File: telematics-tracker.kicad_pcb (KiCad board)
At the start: 4 copper layers, 82 x 62 mm, 227 parts, among them J1 WAFER-MX3.0-12PZZ, J2 B3B-XH-A, Q1 AM2390N-TP, Q10 MMBT3904, Q11 MMBT3904, Q12 MMBT3904, Q13 MMBT3906, Q14 MMBT3904, Q2 AM2390N-TP, Q3 AO3401A, Q4 MMBT3904, Q5 MMBT3904, Q6 MMBT3904, Q7 MMBT3904, Q8 MMBT3904, Q9 MMBT3904, U1 EC200UCNAA-N05-SGNSA, U2 AT32F403ACGT7, U3 QMI8658B, U4 SIT1051AT/3, U5 EG11752, U6 BQ25606RGER, U7 GD25Q64ESIGR, U8 TXB0104PWR, U9 ME6211C33M5G, X1 NANO-SIM, X2 MFF2-eSIM-pads, Y1 8MHz, Y2 32.768kHz

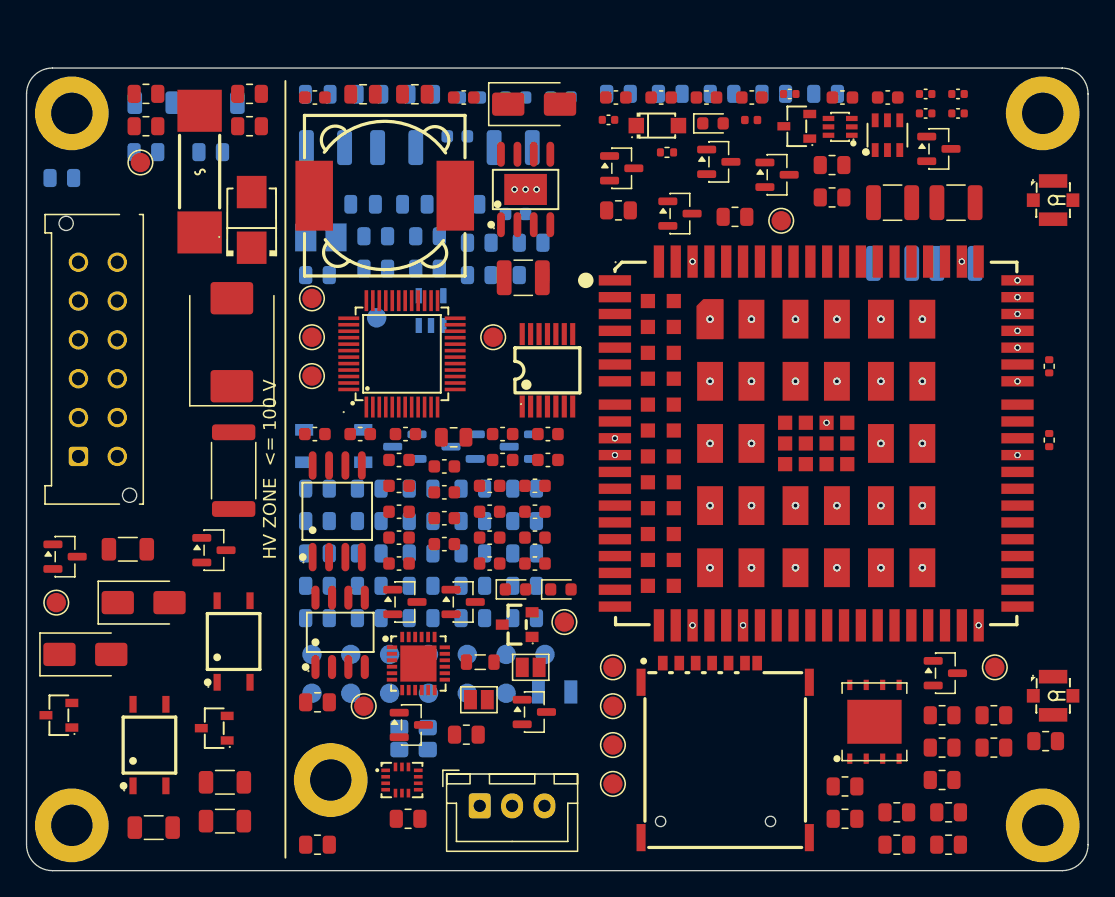
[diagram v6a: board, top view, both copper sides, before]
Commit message: F-21 RETRACTED (my misread); antennas selected; 8 of 8 floorplan checks pass
F-21 was wrong and the error was mine. I read the pdftotext -layout dump, where
0R and 100 pF share a row and NM NM sit below, and took the 100 pF for a shunt.
Rendering page 69 at 200 dpi shows it has VERTICAL plates in the signal line: it
is a SERIES DC BLOCK, and the 47 nH injects VDD on the ANTENNA side of it. The
module pin is DC-isolated by construction; there was never a conflict.
Corroborated by Antenna Design Guide V3.3 5.1 note 5, which also asks for
>= 56 nH - so L4 is 68 nH, not figure 31's 47 nH. Table 40 does not list
ANT_GNSS at all, so there is no published DC rating for pin 47, which is the
real reason the block is mandatory.

Schematic corrected: C84 100 pF is in SERIES and ALWAYS FITTED (depopulating it
opens the antenna; 1.0 ohm at 1575 MHz). Only L4/R90/C83 are DNP. Chain verified
in the netlist: U1.47 -> R72 -> C84 -> AF2.3, bias injected at ANT_GNSS_F.
C84 anchored inline in the RF corridor and check 1 extended to validate every
inline element. checkpins caught a real short while doing this - the first
bias-T placement merged GNSS_BIAS into USIM_VDD.

Parts: C1546 100pF C0G (always fitted), C3221844 Murata LQW15AN68NG80D 68 nH
WIREWOUND SRF 2.5 GHz (every multilayer 0402 at this value has SRF ~1.1 GHz and
is capacitive at 1575 MHz), C25077 10R, C60474 0.1uF.

Antennas: LTE C496569 Bat Wireless BW4GFNX39-15B1, 700-2700 MHz continuous,
120 mm IPEX-1 pigtail, 5536 stock. Runner-up C22467619 rejected - it omits B40,
which Jio uses heavily in India.

GNSS C784386 - but this is a DEVIATION NEEDING A DECISION: no passive 25x25
patch with a U.FL pigtail exists in LCSC stock, so the recommendation is ACTIVE
(LNA 21.5 dB, 1.8-3.6 V, 4.3 mA). That makes the bias-T MANDATORY rather than
DNP for the internal build. Passive alternative C784398 has solder pins and no
cable, needing a hand-added pigtail and a 60-70 mm lid ground plane.

Quectel's < 17 dB LNA limit is a recommendation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
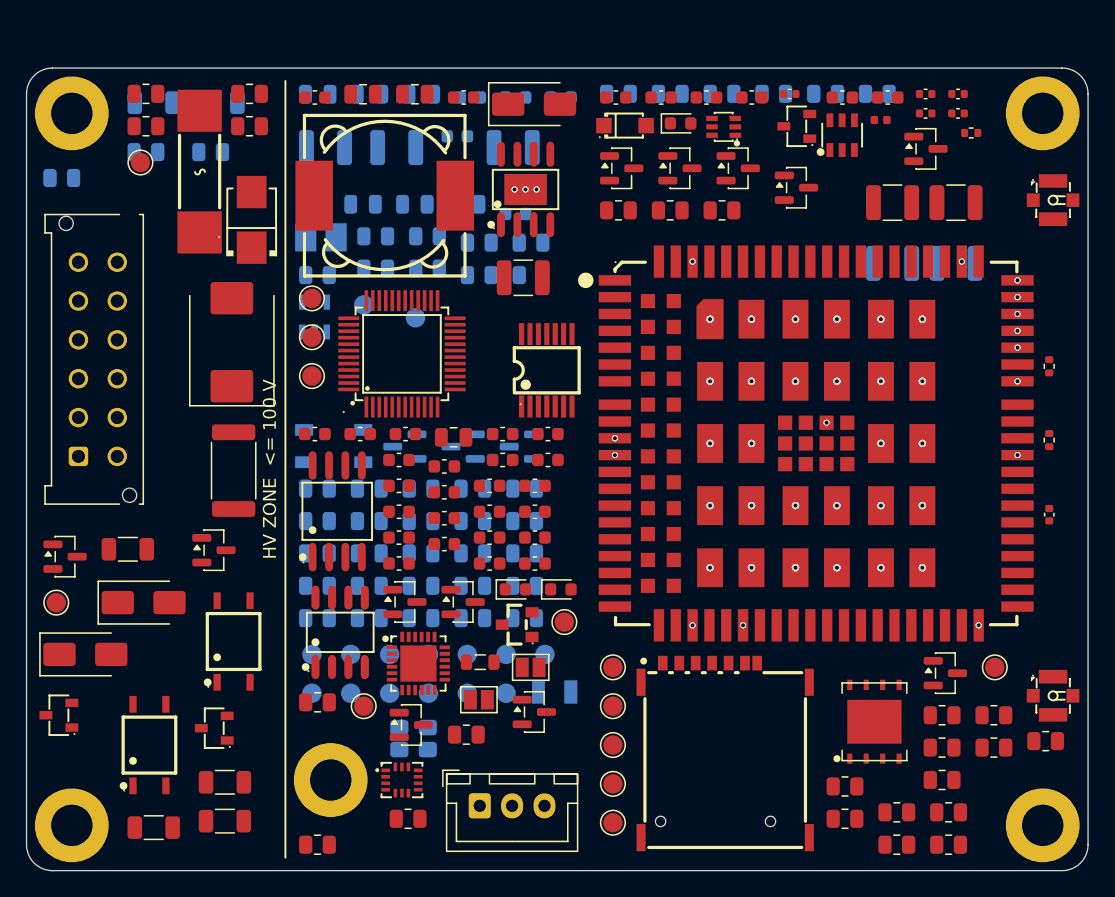
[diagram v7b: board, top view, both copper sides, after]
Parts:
- C83: value 100nF DNP -> 100nF
- C84: value 100pF DNP -> 100pF C0G
- L4: value 47nH DNP -> 68nH
- R65, TP22: moved to B.Cu
- R90: value 10R DNP -> 10R
- moved R65 63.4 mm to (45.7, 2.00), turned to 180 degrees
- moved C84 45.7 mm to (79.0, 34.5), turned to 90 degrees
- moved R53 41.7 mm to (70.7, 50.0)
- moved TP14 36.9 mm to (45.3, 46.3)
- moved TP16 29.7 mm to (45.3, 49.3)
- moved TP15 29.5 mm to (74.8, 46.3)
- moved R90 23.5 mm to (73.0, 5.01)
- moved R50 16.9 mm to (45.7, 11.0)
- moved TP21 14.3 mm to (22.0, 23.8)
- moved R51 12.5 mm to (49.7, 11.0)
- moved L4 10.00 mm to (66.0, 4.01)
- moved Q14 9.22 mm to (59.5, 9.24)
- moved U9 9.01 mm to (22.2, 19.2)
- moved D14 9.00 mm to (53.9, 4.54)
- moved R56 8.02 mm to (70.7, 52.5)
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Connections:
- AF2 pad 3: /modem_rf/ANT_GNSS_C -> /modem_rf/ANT_GNSS_F
- C84 pad 2: GND -> /modem_rf/ANT_GNSS_F
- L4 pad 1: /modem_rf/ANT_GNSS_C -> /modem_rf/ANT_GNSS_F

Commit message: Pre-routing: R90 short protection, bias-T on all builds, F-23 antenna temp
Bias-T POPULATED on all builds - the selected GNSS antenna C784386 is active
(LNA 21.5 dB, 1.8-3.6 V), so L4/R90/C83 are no longer DNP. C84 100pF series DC
block was already always-fitted.

R90 antenna-short current limit = 68R 1210 (F-22). The vendor publishes only a
TYPICAL 4.3 mA and no maximum, so this is designed to a conservative multiple:
  normal, 3V3 at -5%: V_ant = 2.84 V at 1x typical, still 1.95 V at 4x typical
                      (needs >= 1.80 V) - tolerates 4.3x the typical current
  fault, 3V3 at +5%:  50.1 mA into a shorted coax, vs a 500 mA LDO already
                      carrying ~150 mA, and L4 rated 320 mA
  P_R90 in fault:     0.171 W, 68% of a 50%-derated 1210
Deliberately more conservative than the ~150 mA brief: 22R would hit 143 mA but
needs a 2512 and burns 0.448 W CONTINUOUSLY inside a sealed IP65 box at 70 C,
from a fault that does not clear itself. C85 10nF added at the injection node
because 68R (vs Quectel's 10R) raises supply-noise coupling into the LNA.

F-23 NEW - the antennas are the weakest thermal link. Both are -45 to +85 C for
OPERATING AND STORAGE (identical ranges, verified verbatim in both datasheets).
That gives 15 C margin at the +70 C operating limit but ZERO margin at the 85 C
survival limit, with no excursion or derating data published by either vendor.
They are lid-mounted, i.e. in the hottest part of the enclosure. Bench soak at
85 C required before release; decision open on whether to accept, narrow the
survival spec, or treat antennas as serviceable.

Antenna retention must be MECHANICAL - heat stake, clamp, rib or captive pocket,
never adhesive alone (Quectel Antenna Design Guide V3.3 3.1 note 3: adhesive
weakens at high ambient). Added to the installation sheet AND as a housing
selection criterion in handoff 6.3 and 7 - the enclosure must provide the
retention feature, so a plain smooth-lidded box will not do.

Also noted: both datashe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
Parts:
- removed the FB1 at (35.0, 45.9)
- removed the R1 at (22.5, 49.0)
- added D1: S3M, SMB_L4.3-W3.6-LS5.3-RD, F.Cu at (17.4, 11.7)
- added H1: MountingHole_3.2mm_M3_ISO7380_Pad, MountingHole_3.2mm_M3_ISO7380_Pad, F.Cu at (3.50, 3.50)
- added TP1: SWDIO, TestPoint_Pad_D1.5mm, F.Cu at (41.5, 42.8)
- C85: renamed from C9; value 100nF -> 10nF; footprint C_0603_1608Metric -> C_0402_1005Metric
- C9: renamed from D1; value S3M -> 100nF; footprint SMB_L4.3-W3.6-LS5.3-RD -> C_0603_1608Metric
- FB1: renamed from H1; value MountingHole_3.2mm_M3_ISO7380_Pad -> 600R@100MHz; footprint MountingHole_3.2mm_M3_ISO7380_Pad -> L_0805_2012Metric
- R1: renamed from R11; value 60.4R -> 10k
- R12: renamed from R14; value 12k -> 60.4R; footprint R_1206_3216Metric -> R_0805_2012Metric
- R17: renamed from R18; moved to F.Cu
- R19: renamed from R2; value 10k -> 12k; footprint R_0805_2012Metric -> R_1206_3216Metric; moved to B.Cu
- R2: renamed from R21; value 47k -> 10k; moved to F.Cu
- R22: renamed from R23; value 100R -> 47k
- R24: renamed from R25; value 10k -> 100R
- R26: renamed from R3; value 0R -> 10k
- R3: renamed from R30; value 100k -> 0R; moved to B.Cu
- R31: renamed from R32; moved to F.Cu
- R32: renamed from R33; moved to B.Cu
- R34: renamed from R35; moved to F.Cu
- R35: renamed from R36; value 9.1k -> 100k
- R37: renamed from R38; value 1M -> 9.1k
- R39: renamed from R4; value 1k -> 1M
- R4: renamed from R40; value 100k -> 1k
- R40: renamed from R41; value 9.1k -> 100k
- R41: renamed from R42; value 4.7k -> 9.1k
- R42: renamed from R43; value 10k -> 4.7k
- R44: renamed from R45; value 2.2k -> 10k
- R45: renamed from R46; value 4.7k -> 2.2k
- R46: renamed from R47; value 10k -> 4.7k
- R48: renamed from R49; value 2.2k -> 10k
- R49: renamed from R5; value 4.7k -> 2.2k
- R5: renamed from R50; value 100k -> 4.7k; moved to B.Cu
- R50: renamed from R51; value 10k -> 100k
- R51: renamed from R52; value 47k -> 10k
- R52: renamed from R53; value 4.7k -> 47k
- R53: renamed from R54; value 47k -> 4.7k
- R54: renamed from R55; value 4.7k -> 47k
- R55: renamed from R56; value 47k -> 4.7k
- R56: renamed from R57; value 4.7k -> 47k
- R57: renamed from R58; value 47k -> 4.7k
- R58: renamed from R59; value 4.7k -> 47k
- R59: renamed from R6; value 1k -> 4.7k; moved to F.Cu
- R6: renamed from R60; value 47k -> 1k; moved to B.Cu
- R61: renamed from R62; value 10k -> 47k
- R62: renamed from R63; value 47k -> 10k
- R63: renamed from R64; value 4.7k -> 47k
- R64: renamed from R65; value 1k -> 4.7k; moved to F.Cu
- R65: renamed from R66; value 33R -> 1k; moved to F.Cu
- R68: renamed from R69; value 0R -> 33R
- R69: renamed from R7; value 2.2k -> 0R
- R7: renamed from R70; value 0R -> 2.2k
- R70: renamed from R71; footprint R_0402_1005Metric -> R_0805_2012Metric; moved to B.Cu
- R72: renamed from R8; value 2.2k -> 0R; footprint R_0805_2012Metric -> R_0402_1005Metric; moved to F.Cu
- R8: renamed from R80; value 1R 2512 anti-surge -> 2.2k; footprint R_2512_6332Metric -> R_0805_2012Metric; moved to B.Cu
- R80: renamed from R81; value 100k -> 1R 2512 anti-surge; footprint R_0805_2012Metric -> R_2512_6332Metric; moved to F.Cu
- R81: renamed from R82; value 0R (F-12) -> 100k
- R82: renamed from R83; value 4.3k -> 0R (F-12)
- R83: renamed from R84; value 1.5k -> 4.3k
- R84: renamed from R85; value 976R -> 1.5k
- R85: renamed from R86; value 536R -> 976R
- R86: renamed from R87; value 10k -> 536R
- R87: renamed from R88; value 5.23k -> 10k
- R88: renamed from R89; value 30.1k -> 5.23k
- R89: renamed from R90; value 10R -> 30.1k; footprint R_0402_1005Metric -> R_0805_2012Metric; moved to B.Cu
- R90: renamed from TP1; value SWDIO -> 68R; footprint TestPoint_Pad_D1.5mm -> R_1210_3225Metric; moved to B.Cu
- moved R64 61.9 mm to (67.2, 60.0), turned to 0 degrees
- moved R65 61.9 mm to (71.2, 60.0), turned to 0 degrees
- moved R19 57.8 mm to (14.8, 2.67), turned to 180 degrees
- moved R17 56.0 mm to (9.82, 58.7), turned to 0 degrees
- moved FB1 52.8 mm to (35.0, 45.9)
- moved R7 51.2 mm to (34.5, 42.5)
- moved R90 47.2 mm to (66.3, 2.62), turned to 180 degrees
- moved R69 46.7 mm to (57.7, 2.00)
- moved R52 46.3 mm to (45.7, 11.0)
- moved R53 43.4 mm to (54.7, 11.5)
- moved R72 42.8 mm to (79.0, 28.7), turned to 90 degrees
- moved R59 42.1 mm to (70.7, 55.0), turned to 0 degrees
- moved R40 40.1 mm to (2.73, 8.49)
- moved R6 39.7 mm to (30.5, 42.5), turned to 180 degrees
- moved TP14 39.3 mm to (49.8, 7.30)
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- renumbered R12 to R11, R15 to R14, R16 to R15, R17 to R16, R19 to R18, R22 to R21, R24 to R23, R26 to R25, R31 to R30, R34 to R33, R37 to R36, R39 to R38, R44 to R43, R48 to R47, R61 to R60, R67 to R66, R68 to R67, R72 to R71
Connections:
- C85 pad 1: 3V3 -> /modem_rf/GNSS_BIAS
- C9 pad 1: /power/VIN_P -> 3V3
- C9 pad 2: /power/VIN_F -> GND
- FB1 pad 1: GND -> 3V3
- R1 pad 1: /io/CANH_T -> /mcu/BOOT0
- R1 pad 2: /io/CAN_MID -> GND
- R11 pad 1: /io/CANL_T -> /io/CANH_T
- R12 pad 1: /io/DI1_IN -> /io/CANL_T
- R12 pad 2: /io/DI1_M1 -> /io/CAN_MID
- R14 pad 1: /io/DI1_M1 -> /io/DI1_IN
- R14 pad 2: /io/DI1_M2 -> /io/DI1_M1
- R15 pad 1: /io/DI1_M2 -> /io/DI1_M1
- R15 pad 2: /io/DI1_LED -> /io/DI1_M2
- R16 pad 1: /io/DI2_IN -> /io/DI1_M2
- R16 pad 2: /io/DI2_M1 -> /io/DI1_LED
- R17 pad 1: /io/DI2_M1 -> /io/DI2_IN
- R17 pad 2: /io/DI2_M2 -> /io/DI2_M1
- R18 pad 1: /io/DI2_M2 -> /io/DI2_M1
- R18 pad 2: /io/DI2_LED -> /io/DI2_M2
- R19 pad 1: /mcu/BOOT1 -> /io/DI2_M2
- R19 pad 2: GND -> /io/DI2_LED
- R2 pad 1: 3V3 -> /mcu/BOOT1
- R2 pad 2: DI1 -> GND
- R21 pad 2: DI2 -> DI1
- R22 pad 1: /io/DO1_DRV -> 3V3
- R22 pad 2: /io/Q1_G -> DI2
- R23 pad 1: /io/DO2_DRV -> /io/DO1_DRV
- R23 pad 2: /io/Q2_G -> /io/Q1_G
- R24 pad 1: /io/Q1_G -> /io/DO2_DRV
- R24 pad 2: GND -> /io/Q2_G
- R25 pad 1: /io/Q2_G -> /io/Q1_G
- R26 pad 1: 3V3 -> /io/Q2_G
- R26 pad 2: /mcu/VBAT_MCU -> GND
- R3 pad 1: VIN -> 3V3
- R3 pad 2: /io/VIN_D0 -> /mcu/VBAT_MCU
- R30 pad 1: /io/VIN_D0 -> VIN
- R30 pad 2: /io/VIN_D1 -> /io/VIN_D0
- R31 pad 1: /io/VIN_D1 -> /io/VIN_D0
- R31 pad 2: VIN_SENSE -> /io/VIN_D1
- R32 pad 1: /io/IGN -> /io/VIN_D1
- R32 pad 2: /io/IGN_D0 -> VIN_SENSE
- R33 pad 1: /io/IGN_D0 -> /io/IGN
- R33 pad 2: /io/IGN_D1 -> /io/IGN_D0
- R34 pad 1: /io/IGN_D1 -> /io/IGN_D0
- R34 pad 2: IGN_SENSE -> /io/IGN_D1
- R35 pad 1: VIN_SENSE -> /io/IGN_D1
- R35 pad 2: GND -> IGN_SENSE
- R36 pad 1: IGN_SENSE -> VIN_SENSE
- R37 pad 1: SYS -> IGN_SENSE
- R37 pad 2: VBAT_SENSE -> GND
- R38 pad 1: VBAT_SENSE -> SYS
- R38 pad 2: GND -> VBAT_SENSE
- R39 pad 1: 3V3 -> VBAT_SENSE
- R39 pad 2: /mcu/SYS_LED_A -> GND
- R4 pad 1: VIN -> 3V3
- R4 pad 2: ADC_SPARE -> /mcu/SYS_LED_A
- R40 pad 1: ADC_SPARE -> VIN
- R40 pad 2: GND -> ADC_SPARE
- R41 pad 1: DO1_GATE -> ADC_SPARE
- R41 pad 2: /io/DO1_B -> GND
- R42 pad 2: GND -> /io/DO1_B
- R43 pad 1: 5V0 -> DO1_GATE
- R43 pad 2: /io/DO1_X -> GND
- R44 pad 2: /io/DO1_DRV -> /io/DO1_X
- R45 pad 1: DO2_GATE -> 5V0
- R45 pad 2: /io/DO2_B -> /io/DO1_DRV
- R46 pad 2: GND -> /io/DO2_B
- R47 pad 1: 5V0 -> DO2_GATE
- R47 pad 2: /io/DO2_X -> GND
- R48 pad 2: /io/DO2_DRV -> /io/DO2_X
- R49 pad 1: /mcu/NET_STATUS_LED -> 5V0
- R49 pad 2: /mcu/NSL_BASE -> /io/DO2_DRV
- R5 pad 1: /modem_rf/Q3_G -> /mcu/NET_STATUS_LED
- R5 pad 2: GND -> /mcu/NSL_BASE
- R50 pad 1: /modem_rf/Q13_B -> /modem_rf/Q3_G
- R50 pad 2: /modem_rf/Q14_C -> GND
- R51 pad 1: SYS -> /modem_rf/Q13_B
- R51 pad 2: /modem_rf/Q13_B -> /modem_rf/Q14_C
- R52 pad 1: MODEM_PWR_EN -> SYS
- R52 pad 2: /modem_rf/Q14_B -> /modem_rf/Q13_B
- R53 pad 1: /modem_rf/Q14_B -> MODEM_PWR_EN
- R53 pad 2: GND -> /modem_rf/Q14_B
- R54 pad 1: MODEM_PWRKEY -> /modem_rf/Q14_B
- R54 pad 2: /modem_rf/Q9_B -> GND
- R55 pad 1: /modem_rf/Q9_B -> MODEM_PWRKEY
- R55 pad 2: GND -> /modem_rf/Q9_B
- R56 pad 1: MODEM_RESET -> /modem_rf/Q9_B
- R56 pad 2: /modem_rf/Q10_B -> GND
- R57 pad 1: /modem_rf/Q10_B -> MODEM_RESET
- R57 pad 2: GND -> /modem_rf/Q10_B
- R58 pad 1: /modem_rf/STATUS_MOD -> /modem_rf/Q10_B
- R58 pad 2: /modem_rf/Q11_B -> GND
- R59 pad 1: 3V3 -> /modem_rf/STATUS_MOD
- R59 pad 2: /mcu/NSL_A -> /modem_rf/Q11_B
- R6 pad 1: /modem_rf/Q11_B -> 3V3
- R6 pad 2: GND -> /mcu/NSL_A
- R60 pad 1: 3V3 -> /modem_rf/Q11_B
- R60 pad 2: MODEM_STATUS -> GND
- R61 pad 1: /modem_rf/U8_OE -> 3V3
- R61 pad 2: GND -> MODEM_STATUS
- R62 pad 1: /modem_rf/VDD_EXT_1V8 -> /modem_rf/U8_OE
- R62 pad 2: /modem_rf/U8_OE -> GND
- R63 pad 1: /modem_rf/NETLIGHT_MOD -> /modem_rf/VDD_EXT_1V8
- R63 pad 2: /modem_rf/Q12_B -> /modem_rf/U8_OE
- R64 pad 1: 3V3 -> /modem_rf/NETLIGHT_MOD
- R64 pad 2: /modem_rf/NETLED_A -> /modem_rf/Q12_B
- R65 pad 1: /modem_rf/USIM_DATA_M -> 3V3
- R65 pad 2: /modem_rf/SIM_DATA -> /modem_rf/NETLED_A
- R66 pad 1: /modem_rf/USIM_CLK_M -> /modem_rf/USIM_DATA_M
- R66 pad 2: /modem_rf/SIM_CLK -> /modem_rf/SIM_DATA
- R67 pad 1: /modem_rf/USIM_RST_M -> /modem_rf/USIM_CLK_M
- R67 pad 2: /modem_rf/SIM_RST -> /modem_rf/SIM_CLK
- R68 pad 1: /modem_rf/USIM_VDD -> /modem_rf/USIM_RST_M
- R68 pad 2: /modem_rf/USIM_VDD_SIM -> /modem_rf/SIM_RST
- R69 pad 1: 3V3 -> /modem_rf/USIM_VDD
- R69 pad 2: /mcu/I2C1_SCL -> /modem_rf/USIM_VDD_SIM
- R7 pad 1: /modem_rf/USIM_VDD -> 3V3
- R7 pad 2: /modem_rf/USIM_VDD_ESIM -> /mcu/I2C1_SCL
- R70 pad 1: /modem_rf/ANT_MAIN_M -> /modem_rf/USIM_VDD
- R70 pad 2: /modem_rf/ANT_MAIN_C -> /modem_rf/USIM_VDD_ESIM
- R71 pad 1: /modem_rf/ANT_GNSS_M -> /modem_rf/ANT_MAIN_M
- R71 pad 2: /modem_rf/ANT_GNSS_C -> /modem_rf/ANT_MAIN_C
- R72 pad 1: 3V3 -> /modem_rf/ANT_GNSS_M
- R72 pad 2: /mcu/I2C1_SDA -> /modem_rf/ANT_GNSS_C
- R8 pad 1: /power/VIN_P -> 3V3
- R8 pad 2: /power/VIN_B -> /mcu/I2C1_SDA
- R80 pad 1: /power/U5_VCC -> /power/VIN_P
- R80 pad 2: /power/U5_EN -> /power/VIN_B
- R81 pad 1: /power/U5_IS -> /power/U5_VCC
- R81 pad 2: /power/SW_BUCK -> /power/U5_EN
- R82 pad 1: 5V0 -> /power/U5_IS
- R82 pad 2: /power/U5_FB -> /power/SW_BUCK
- R83 pad 1: /power/U5_FB -> 5V0
- R83 pad 2: GND -> /power/U5_FB
- R84 pad 1: /power/U6_ICHG -> /power/U5_FB
- R85 pad 1: /power/U6_ILIM -> /power/U6_ICHG
- R86 pad 1: /power/U6_OTG -> /power/U6_ILIM
- R87 pad 1: /power/REGN -> /power/U6_OTG
- R87 pad 2: /power/U6_TS -> GND
- R88 pad 1: /power/U6_TS -> /power/REGN
- R88 pad 2: GND -> /power/U6_TS
- R89 pad 1: 3V3 -> /power/U6_TS
- R89 pad 2: /modem_rf/GNSS_BIAS -> GND
- R90 pad 1: /mcu/SWDIO -> 3V3
